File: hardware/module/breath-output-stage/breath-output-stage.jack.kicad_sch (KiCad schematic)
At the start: 3 parts

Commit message: WIP module schematics: footprints, bought-part fields, and the two board projects (module-main, module-jack)
Recovered from a container restart; not yet exported or checked.

Co-Authored-By: Claude Opus 5.5 <noreply@anthropic.com>
Claude-Session: https://claude.ai/code/session_01LmB4muFXnoLprWX4JzuJ5A
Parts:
- J-CV-BREATH: footprint (none) -> Connector_Audio:Jack_3.5mm_QingPu_WQP-PJ398SM_Vertical_CircularHoles; Assembly (none) -> hand; MPN (none) -> PJ398SM; Manufacturer (none) -> Thonk
- POT-GAIN: footprint (none) -> woody:Potentiometer_SongHuei_R0904N_Single_Vertical; Assembly (none) -> hand; MPN (none) -> R0904N-B50K; Manufacturer (none) -> Song Huei
- POT-OFFSET: footprint (none) -> woody:Potentiometer_SongHuei_R0904N_Single_Vertical; Assembly (none) -> hand; MPN (none) -> R0904N-B10K; Manufacturer (none) -> Song Huei
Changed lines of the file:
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@@
     (property "Reference" "POT-GAIN" (at 40.64 43.18 0) (effects (font (size 1.27 1.27))))
     (property "Value" "50k" (at 40.64 45.72 0) (effects (font (size 1.27 1.27))))
-    (property "Footprint" "" (at 40.64 50.8 0) (effects (font (size 1.27 1.27)) hide))
+    (property "Footprint" "woody:Potentiometer_SongHuei_R0904N_Single_Vertical" (at 40.64 50.8 0) (effects (font (size 1.27 1.27)) hide))
     (property "Datasheet" "" (at 40.64 50.8 0) (effects (font (size 1.27 1.27)) hide))
     (property "Row" "POT-GAIN" (at 40.64 50.8 0) (effects (font (size 1.27 1.27)) hide))
@@
     (property "Note" "Attenuator, not a feedback rheostat. 0.125 to 1.000 with R-GAIN-FLOOR" (at 40.64 50.8 0) (effects (font (size 1.27 1.27)) hide))
     (property "Pins_source" "datasheets/connectors/R0904N.pdf p.2 (drawing R09N-003): pins 1-2-3, 2 the wiper, shaft drawn full CCW; clockwise toward 3 is the usual convention [from memory]" (at 40.64 50.8 0) (effects (font (size 1.27 1.27)) hide))
+    (property "Manufacturer" "Song Huei" (at 40.64 50.8 0) (effects (font (size 1.27 1.27)) hide))
+    (property "MPN" "R0904N-B50K" (at 40.64 50.8 0) (effects (font (size 1.27 1.27)) hide))
+    (property "LCSC" "" (at 40.64 50.8 0) (effects (font (size 1.27 1.27)) hide))
+    (property "Assembly" "hand" (at 40.64 50.8 0) (effects (font (size 1.27 1.27)) hide))
     (pin "1")
     (pin "2")
     (pin "3")
-    (instances (project "breath-output-stage.jack" (path "/9a361b54-43b2-59f7-80b5-953311d0f986" (reference "POT-GAIN") (unit 1))) (project "breath-output-stage" (path "/6f4edadb-6257-58e5-9d51-bec8cbdf5df0/1baad570-1274-5418-a0cf-a0e799c92a9f" (reference "POT-GAIN") (unit 1))))
+    (instances (project "module-jack" (path "/f69c67ba-c380-5393-90d5-6d2847e300fb/8c2d4c65-2fdf-59f6-a0a5-075d84002617" (reference "RV1") (unit 1))) (project "breath-output-stage.jack" (path "/9a361b54-43b2-59f7-80b5-953311d0f986" (reference "POT-GAIN") (unit 1))) (project "breath-output-stage" (path "/6f4edadb-6257-58e5-9d51-bec8cbdf5df0/1baad570-1274-5418-a0cf-a0e799c92a9f" (reference "POT-GAIN") (unit 1))))
   )
   (symbol (lib_id "Device:R_Potentiometer") (at 91.44 50.8 0) (unit 1)
@@
     (property "Reference" "POT-OFFSET" (at 91.44 43.18 0) (effects (font (size 1.27 1.27))))
     (property "Value" "10k linear" (at 91.44 45.72 0) (effects (font (size 1.27 1.27))))
-    (property "Footprint" "" (at 91.44 50.8 0) (effects (font (size 1.27 1.27)) hide))
+    (property "Footprint" "woody:Potentiometer_SongHuei_R0904N_Single_Vertical" (at 91.44 50.8 0) (effects (font (size 1.27 1.27)) hide))
     (property "Datasheet" "" (at 91.44 50.8 0) (effects (font (size 1.27 1.27)) hide))
     (property "Row" "POT-OFFSET" (at 91.44 50.8 0) (effects (font (size 1.27 1.27)) hide))
@@
     (property "Note" "Wiper UNBUFFERED - its R/4 source impedance is why zero sits ~20 deg past centre" (at 91.44 50.8 0) (effects (font (size 1.27 1.27)) hide))
     (property "Pins_source" "datasheets/connectors/R0904N.pdf p.2 (drawing R09N-003): pins 1-2-3, 2 the wiper, shaft drawn full CCW; clockwise toward 3 is the usual convention [from memory]" (at 91.44 50.8 0) (effects (font (size 1.27 1.27)) hide))
+    (property "Manufacturer" "Song Huei" (at 91.44 50.8 0) (effects (font (size 1.27 1.27)) hide))
+    (property "MPN" "R0904N-B10K" (at 91.44 50.8 0) (effects (font (size 1.27 1.27)) hide))
+    (property "LCSC" "" (at 91.44 50.8 0) (effects (font (size 1.27 1.27)) hide))
+    (property "Assembly" "hand" (at 91.44 50.8 0) (effects (font (size 1.27 1.27)) hide))
     (pin "1")
     (pin "2")
     (pin "3")
-    (instances (project "breath-output-stage.jack" (path "/9a361b54-43b2-59f7-80b5-953311d0f986" (reference "POT-OFFSET") (unit 1))) (project "breath-output-stage" (path "/6f4edadb-6257-58e5-9d51-bec8cbdf5df0/1baad570-1274-5418-a0cf-a0e799c92a9f" (reference "POT-OFFSET") (unit 1))))
+    (instances (project "module-jack" (path "/f69c67ba-c380-5393-90d5-6d2847e300fb/8c2d4c65-2fdf-59f6-a0a5-075d84002617" (reference "RV2") (unit 1))) (project "breath-output-stage.jack" (path "/9a361b54-43b2-59f7-80b5-953311d0f986" (reference "POT-OFFSET") (unit 1))) (project "breath-output-stage" (path "/6f4edadb-6257-58e5-9d51-bec8cbdf5df0/1baad570-1274-5418-a0cf-a0e799c92a9f" (reference "POT-OFFSET") (unit 1))))
   )
   (symbol (lib_id "Connector_Audio:AudioJack2") (at 142.24 50.8 0) (unit 1)
@@
     (property "Reference" "J-CV-BREATH" (at 144.78 49.53 0) (effects (font (size 1.27 1.27)) (justify left)))
     (property "Value" "PJ398SM" (at 144.78 52.07 0) (effects (font (size 1.27 1.27)) (justify left)))
-    (property "Footprint" "" (at 142.24 50.8 0) (effects (font (size 1.27 1.27)) hide))
+    (property "Footprint" "Connector_Audio:Jack_3.5mm_QingPu_WQP-PJ398SM_Vertical_CircularHoles" (at 142.24 50.8 0) (effects (font (size 1.27 1.27)) hide))
     (property "Datasheet" "" (at 142.24 50.8 0) (effects (font (size 1.27 1.27)) hide))
     (property "Row" "J-CV" (at 142.24 50.8 0) (effects (font (size 1.27 1.27)) hide))
@@
     (property "Note" "THE JACK IS THIS CIRCUIT'S PART - module/panel owns the hole. Third pin, the normalling contact, unused" (at 142.24 50.8 0) (effects (font (size 1.27 1.27)) hide))
     (property "Pins_source" "datasheets/connectors/PJ398SM.kicad_mod pad names T, TN, S; datasheets/connectors/PJ398SM-drawing.jpg: 3 tip, 2 normalling contact, 1 sleeve. TN is not on this symbol: unused, not netted" (at 142.24 50.8 0) (effects (font (size 1.27 1.27)) hide))
+    (property "Manufacturer" "Thonk" (at 142.24 50.8 0) (effects (font (size 1.27 1.27)) hide))
+    (property "MPN" "PJ398SM" (at 142.24 50.8 0) (effects (font (size 1.27 1.27)) hide))
+    (property "LCSC" "" (at 142.24 50.8 0) (effects (font (size 1.27 1.27)) hide))
+    (property "Assembly" "hand" (at 142.24 50.8 0) (effects (font (size 1.27 1.27)) hide))
     (pin "S")
     (pin "T")
-    (instances (project "breath-output-stage.jack" (path "/9a361b54-43b2-59f7-80b5-953311d0f986" (reference "J-CV-BREATH") (unit 1))) (project "breath-output-stage" (path "/6f4edadb-6257-58e5-9d51-bec8cbdf5df0/1baad570-1274-5418-a0cf-a0e799c92a9f" (reference "J-CV-BREATH") (unit 1))))
+    (instances (project "module-jack" (path "/f69c67ba-c380-5393-90d5-6d2847e300fb/8c2d4c65-2fdf-59f6-a0a5-075d84002617" (reference "J2") (unit 1))) (project "breath-output-stage.jack" (path "/9a361b54-43b2-59f7-80b5-953311d0f986" (reference "J-CV-BREATH") (unit 1))) (project "breath-output-stage" (path "/6f4edadb-6257-58e5-9d51-bec8cbdf5df0/1baad570-1274-5418-a0cf-a0e799c92a9f" (reference "J-CV-BREATH") (unit 1))))
   )
   (wire (pts (xy 40.64 54.61) (xy 40.64 57.15)) (stroke (width 0) (type default)))

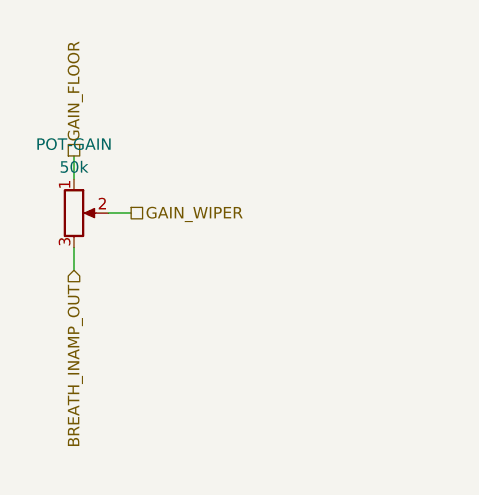
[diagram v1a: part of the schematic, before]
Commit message: Breath response shaper adopted: restoring half drawn, output feeds POT-GAIN; pots ordered to fit the knob
U-RESP B restores x2 inverting (R-RESTORE-IN 10k, R-RESTORE-FB 20k): unity and
the in-amp's polarity at centre detent. BREATH_SHAPED feeds POT-GAIN on
J-B2B-MOD pin 1; nets.yaml moves the shaper from proposed to fitted.
POT-GAIN linear (the design's working gain sits at noon); POT-OFFSET gets no
detent. POT-GAIN/OFFSET are Song Huei R0904N KC (18-tooth, the T18 knob's
shaft; KQ is 40-tooth); POT-RESP Alpha RV09AF-40-25B-B50K-0C (18-tooth B shaft,
centre click). POT-OFFSET's zero is +18.7 deg on the 280-deg track, not 300.

Co-Authored-By: Claude Opus 5.5 <noreply@anthropic.com>
Claude-Session: https://claude.ai/code/session_01LmB4muFXnoLprWX4JzuJ5A
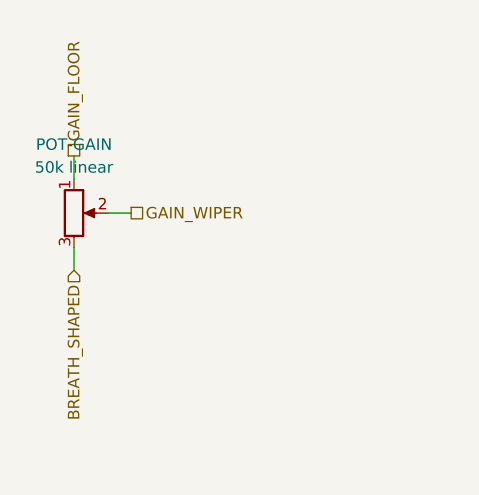
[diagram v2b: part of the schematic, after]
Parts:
- POT-GAIN: value 50k -> 50k linear; MPN R0904N-B50K -> R0904N-B50K L-25 KC
- POT-OFFSET: MPN R0904N-B10K -> R0904N-B10K L-25 KC; Note Wiper UNBUFFERED - its R/4 source impedance is why zero sits ~20 deg past centre -> Wiper UNBUFFERED - its R/4 source impedance is why zero sits ~19 deg past centre on the 280 deg track; no centre detent for that reason
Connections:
- net BREATH_INAMP_OUT renamed BREATH_SHAPED
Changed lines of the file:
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@@
     (in_bom yes) (on_board yes) (dnp no)
     (property "Reference" "POT-GAIN" (at 40.64 43.18 0) (effects (font (size 1.27 1.27))))
-    (property "Value" "50k" (at 40.64 45.72 0) (effects (font (size 1.27 1.27))))
+    (property "Value" "50k linear" (at 40.64 45.72 0) (effects (font (size 1.27 1.27))))
     (property "Footprint" "woody:Potentiometer_SongHuei_R0904N_Single_Vertical" (at 40.64 50.8 0) (effects (font (size 1.27 1.27)) hide))
     (property "Datasheet" "" (at 40.64 50.8 0) (effects (font (size 1.27 1.27)) hide))
@@
     (property "Pins_source" "datasheets/connectors/R0904N.pdf p.2 (drawing R09N-003): pins 1-2-3, 2 the wiper, shaft drawn full CCW; clockwise toward 3 is the usual convention [from memory]" (at 40.64 50.8 0) (effects (font (size 1.27 1.27)) hide))
     (property "Manufacturer" "Song Huei" (at 40.64 50.8 0) (effects (font (size 1.27 1.27)) hide))
-    (property "MPN" "R0904N-B50K" (at 40.64 50.8 0) (effects (font (size 1.27 1.27)) hide))
+    (property "MPN" "R0904N-B50K L-25 KC" (at 40.64 50.8 0) (effects (font (size 1.27 1.27)) hide))
     (property "LCSC" "" (at 40.64 50.8 0) (effects (font (size 1.27 1.27)) hide))
     (property "Assembly" "hand" (at 40.64 50.8 0) (effects (font (size 1.27 1.27)) hide))
@@
     (property "Row" "POT-OFFSET" (at 91.44 50.8 0) (effects (font (size 1.27 1.27)) hide))
     (property "Pins" "CW=3(3) W=2(2) CCW=1(1)" (at 91.44 50.8 0) (effects (font (size 1.27 1.27)) hide))
-    (property "Note" "Wiper UNBUFFERED - its R/4 source impedance is why zero sits ~20 deg past centre" (at 91.44 50.8 0) (effects (font (size 1.27 1.27)) hide))
+    (property "Note" "Wiper UNBUFFERED - its R/4 source impedance is why zero sits ~19 deg past centre on the 280 deg track; no centre detent for that reason" (at 91.44 50.8 0) (effects (font (size 1.27 1.27)) hide))
     (property "Pins_source" "datasheets/connectors/R0904N.pdf p.2 (drawing R09N-003): pins 1-2-3, 2 the wiper, shaft drawn full CCW; clockwise toward 3 is the usual convention [from memory]" (at 91.44 50.8 0) (effects (font (size 1.27 1.27)) hide))
     (property "Manufacturer" "Song Huei" (at 91.44 50.8 0) (effects (font (size 1.27 1.27)) hide))
-    (property "MPN" "R0904N-B10K" (at 91.44 50.8 0) (effects (font (size 1.27 1.27)) hide))
+    (property "MPN" "R0904N-B10K L-25 KC" (at 91.44 50.8 0) (effects (font (size 1.27 1.27)) hide))
     (property "LCSC" "" (at 91.44 50.8 0) (effects (font (size 1.27 1.27)) hide))
     (property "Assembly" "hand" (at 91.44 50.8 0) (effects (font (size 1.27 1.27)) hide))
@@
   )
   (wire (pts (xy 40.64 54.61) (xy 40.64 57.15)) (stroke (width 0) (type default)))
-  (hierarchical_label "BREATH_INAMP_OUT" (shape input) (at 40.64 57.15 270) (effects (font (size 1.27 1.27)) (justify right))
+  (hierarchical_label "BREATH_SHAPED" (shape input) (at 40.64 57.15 270) (effects (font (size 1.27 1.27)) (justify right))
     (property "Dir" "in" (at 40.64 57.15 0) (effects (font (size 1.27 1.27)) hide))
-    (property "From" "module/breath-receive-stage" (at 40.64 57.15 0) (effects (font (size 1.27 1.27)) hide))
-    (property "Note" "0 to inamp-full-scale, rest at 0" (at 40.64 57.15 0) (effects (font (size 1.27 1.27)) hide)))
+    (property "From" "module/breath-response-shaper" (at 40.64 57.15 0) (effects (font (size 1.27 1.27)) hide))
+    (property "Note" "The in-amp's output after the response shaper: equal to it at centre detent" (at 40.64 57.15 0) (effects (font (size 1.27 1.27)) hide)))
   (wire (pts (xy 40.64 46.99) (xy 40.64 44.45)) (stroke (width 0) (type default)))
   (hierarchical_label "GAIN_FLOOR" (shape passive) (at 40.64 44.45 90) (effects (font (size 1.27 1.27)) (justify left))

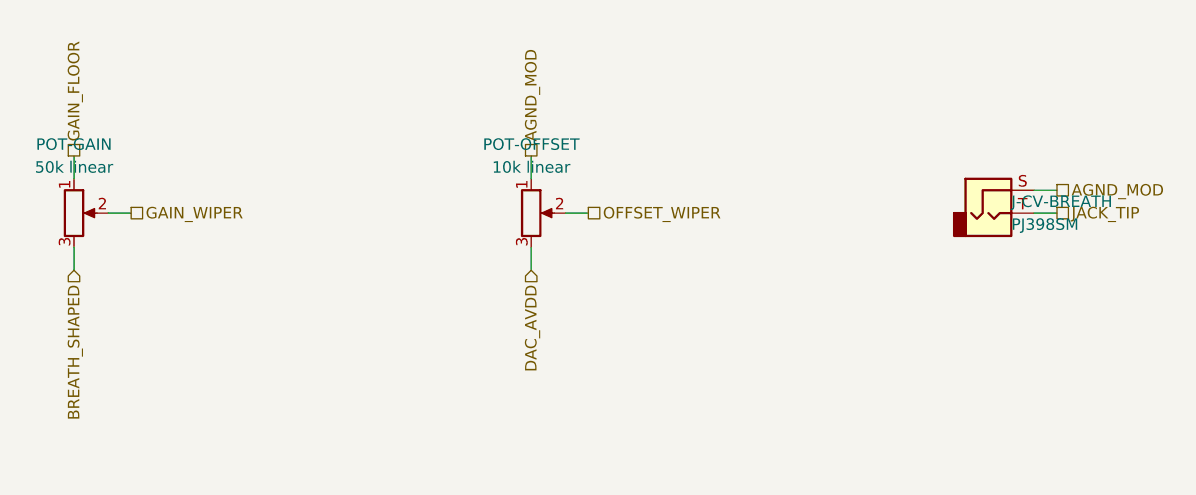
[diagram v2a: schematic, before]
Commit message: Breath chain fixes (pre-layout review A1): OFFSET clockwise-positive, 1N4448W, chain sim, stale derived statements
POT-OFFSET's ends swapped on the sheet so the panel's + is true (A1-4).
D-RESP bought as Vishay 1N4448W-E3-08, datasheet banked (A1-3, owner).
Shaper-into-output-stage sim added; breath-chain-curve-clip registered (A1-1).
Working point cited as disputed (A1-6, A8-4); REF band, ADR 0006 standing
level, C_cm in the pole, R1b dispute, -12 V row, buffered label, ADC
injection current corrected (A1-8..A1-15). Sims re-run pending.

Co-Authored-By: Claude Opus 5.5 <noreply@anthropic.com>
Claude-Session: https://claude.ai/code/session_01LmB4muFXnoLprWX4JzuJ5A
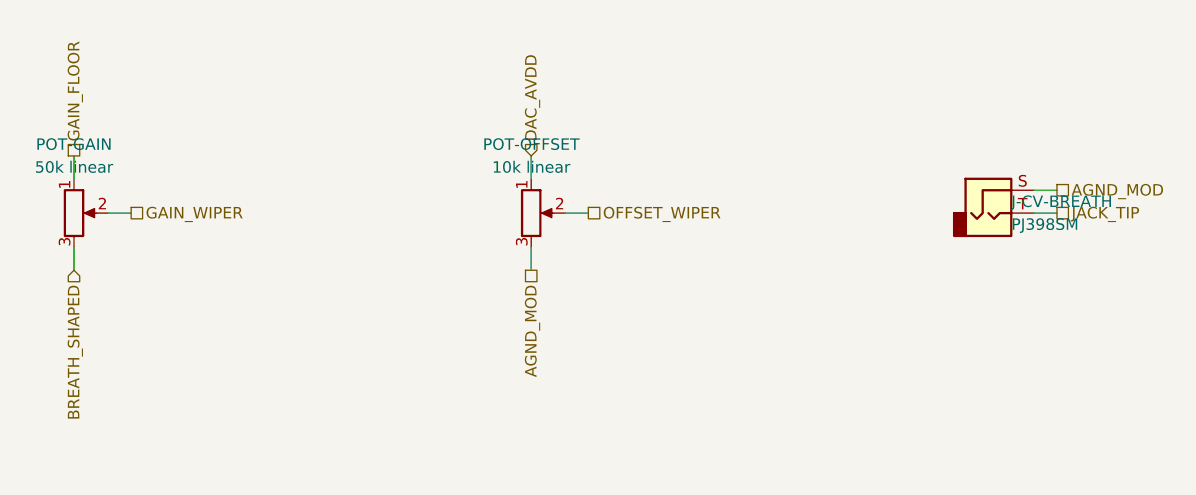
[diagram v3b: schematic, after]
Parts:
- POT-OFFSET: Note Wiper UNBUFFERED - its R/4 source impedance is why zero sit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 -> CW end on AGND_MOD and CCW end on DAC_AVDD, so clockwise mo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
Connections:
- net AGND_MOD: now also POT-OFFSET.3; no longer POT-OFFSET.1
- net DAC_AVDD: now also POT-OFFSET.1; no longer POT-OFFSET.3
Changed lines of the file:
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@@
     (property "Row" "POT-OFFSET" (at 91.44 50.8 0) (effects (font (size 1.27 1.27)) hide))
     (property "Pins" "CW=3(3) W=2(2) CCW=1(1)" (at 91.44 50.8 0) (effects (font (size 1.27 1.27)) hide))
-    (property "Note" "Wiper UNBUFFERED - its R/4 source impedance is why zero sits ~19 deg past centre on the 280 deg track; no centre detent for that reason" (at 91.44 50.8 0) (effects (font (size 1.27 1.27)) hide))
+    (property "Note" "CW end on AGND_MOD and CCW end on DAC_AVDD, so clockwise moves the jack POSITIVE through the inverting summer, as the panel's + mark says (swapped 2026-10-01, A1-4). Wiper UNBUFFERED - its R/4 source impedance is why zero sits ~19 deg counter-clockwise of centre on the 280 deg track; no centre detent for that reason" (at 91.44 50.8 0) (effects (font (size 1.27 1.27)) hide))
     (property "Pins_source" "datasheets/connectors/R0904N.pdf p.2 (drawing R09N-003): pins 1-2-3, 2 the wiper, shaft drawn full CCW; clockwise toward 3 is the usual convention [from memory]" (at 91.44 50.8 0) (effects (font (size 1.27 1.27)) hide))
     (property "Manufacturer" "Song Huei" (at 91.44 50.8 0) (effects (font (size 1.27 1.27)) hide))
@@
     (property "Dir" "ref" (at 46.99 50.8 0) (effects (font (size 1.27 1.27)) hide)))
   (wire (pts (xy 91.44 54.61) (xy 91.44 57.15)) (stroke (width 0) (type default)))
-  (hierarchical_label "DAC_AVDD" (shape input) (at 91.44 57.15 270) (effects (font (size 1.27 1.27)) (justify right))
-    (property "Dir" "in" (at 91.44 57.15 0) (effects (font (size 1.27 1.27)) hide))
-    (property "From" "module/power-entry" (at 91.44 57.15 0) (effects (font (size 1.27 1.27)) hide))
-    (property "Figure" "dac-rail" (at 91.44 57.15 0) (effects (font (size 1.27 1.27)) hide)))
+  (hierarchical_label "DAC_AVDD" (shape input) (at 91.44 44.45 90) (effects (font (size 1.27 1.27)) (justify left))
+    (property "Dir" "in" (at 91.44 44.45 0) (effects (font (size 1.27 1.27)) hide))
+    (property "From" "module/power-entry" (at 91.44 44.45 0) (effects (font (size 1.27 1.27)) hide))
+    (property "Figure" "dac-rail" (at 91.44 44.45 0) (effects (font (size 1.27 1.27)) hide)))
   (wire (pts (xy 95.25 50.8) (xy 97.79 50.8)) (stroke (width 0) (type default)))
   (hierarchical_label "OFFSET_WIPER" (shape passive) (at 97.79 50.8 0) (effects (font (size 1.27 1.27)) (justify left))
@@
     (property "Dir" "ref" (at 149.86 50.8 0) (effects (font (size 1.27 1.27)) hide)))
   (wire (pts (xy 91.44 46.99) (xy 91.44 44.45)) (stroke (width 0) (type default)))
-  (hierarchical_label "AGND_MOD" (shape passive) (at 91.44 44.45 90) (effects (font (size 1.27 1.27)) (justify left))
-    (property "Dir" "ref" (at 91.44 44.45 0) (effects (font (size 1.27 1.27)) hide))
-    (property "From" "module/power-entry" (at 91.44 44.45 0) (effects (font (size 1.27 1.27)) hide)))
+  (hierarchical_label "AGND_MOD" (shape passive) (at 91.44 57.15 270) (effects (font (size 1.27 1.27)) (justify right))
+    (property "Dir" "ref" (at 91.44 57.15 0) (effects (font (size 1.27 1.27)) hide))
+    (property "From" "module/power-entry" (at 91.44 57.15 0) (effects (font (size 1.27 1.27)) hide)))
   (wire (pts (xy 147.32 48.26) (xy 149.86 48.26)) (stroke (width 0) (type default)))
   (hierarchical_label "AGND_MOD" (shape passive) (at 149.86 48.26 0) (effects (font (size 1.27 1.27)) (justify left))
